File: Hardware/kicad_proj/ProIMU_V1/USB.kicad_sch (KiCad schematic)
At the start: 8 parts

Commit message: Updated Schematic and Layout
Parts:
- gave numbers to parts that had none: 8
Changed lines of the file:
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@@
   (symbol (lib_id "power:GND") (at 156.21 92.71 0) (unit 1)
     (in_bom yes) (on_board yes) (fields_autoplaced)
-    (property "Reference" "#PWR?" (id 0) (at 156.21 99.06 0)
+    (property "Reference" "#PWR0104" (id 0) (at 156.21 99.06 0)
       (effects (font (size 1.27 1.27)) hide)
     )
@@
   (symbol (lib_id "power:GND") (at 168.91 64.77 90) (mirror x) (unit 1)
     (in_bom yes) (on_board yes) (fields_autoplaced)
-    (property "Reference" "#PWR?" (id 0) (at 175.26 64.77 0)
+    (property "Reference" "#PWR0102" (id 0) (at 175.26 64.77 0)
       (effects (font (size 1.27 1.27)) hide)
     )
@@
   (symbol (lib_id "power:GND") (at 167.64 57.15 0) (unit 1)
     (in_bom yes) (on_board yes) (fields_autoplaced)
-    (property "Reference" "#PWR?" (id 0) (at 167.64 63.5 0)
+    (property "Reference" "#PWR0103" (id 0) (at 167.64 63.5 0)
       (effects (font (size 1.27 1.27)) hide)
     )
@@
   (symbol (lib_id "power:GND") (at 170.18 91.44 0) (unit 1)
     (in_bom yes) (on_board yes) (fields_autoplaced)
-    (property "Reference" "#PWR?" (id 0) (at 170.18 97.79 0)
+    (property "Reference" "#PWR0105" (id 0) (at 170.18 97.79 0)
       (effects (font (size 1.27 1.27)) hide)
     )
@@
   (symbol (lib_id "Device:R_Small") (at 167.64 50.8 0) (mirror x) (unit 1)
     (in_bom yes) (on_board yes)
-    (property "Reference" "R?" (id 0) (at 165.1 52.07 90)
+    (property "Reference" "R5" (id 0) (at 165.1 52.07 90)
       (effects (font (size 1.27 1.27)) (justify right))
     )
@@
   (symbol (lib_id "Simulation_SPICE:DIODE") (at 179.07 38.1 0) (unit 1)
     (in_bom yes) (on_board yes) (fields_autoplaced)
-    (property "Reference" "D?" (id 0) (at 179.07 31.75 0))
+    (property "Reference" "D2" (id 0) (at 179.07 31.75 0))
     (property "Value" "DIODE" (id 1) (at 179.07 34.29 0))
     (property "Footprint" "" (id 2) (at 179.07 38.1 0)
@@
   (symbol (lib_id "power:VDD") (at 193.04 34.29 0) (mirror y) (unit 1)
     (in_bom yes) (on_board yes)
-    (property "Reference" "#PWR?" (id 0) (at 193.04 38.1 0)
+    (property "Reference" "#PWR0101" (id 0) (at 193.04 38.1 0)
       (effects (font (size 1.27 1.27)) hide)
     )
@@
   (symbol (lib_id "Device:R_Small") (at 167.64 43.18 0) (mirror x) (unit 1)
     (in_bom yes) (on_board yes)
-    (property "Reference" "R?" (id 0) (at 165.1 44.45 90)
+    (property "Reference" "R4" (id 0) (at 165.1 44.45 90)
       (effects (font (size 1.27 1.27)) (justify right))
     )
@@
   (symbol (lib_id "Device:R_Small") (at 154.94 71.12 90) (mirror x) (unit 1)
     (in_bom yes) (on_board yes)
-    (property "Reference" "R?" (id 0) (at 149.86 68.58 90)
+    (property "Reference" "R1" (id 0) (at 149.86 68.58 90)
       (effects (font (size 1.27 1.27)) (justify right))
     )
@@
   (symbol (lib_id "Device:C_Small") (at 160.02 64.77 270) (unit 1)
     (in_bom yes) (on_board yes)
-    (property "Reference" "C?" (id 0) (at 158.75 63.5 90)
+    (property "Reference" "C2" (id 0) (at 158.75 63.5 90)
       (effects (font (size 1.27 1.27)) (justify right))
     )
@@
   (symbol (lib_id "Power_Protection:SP0502BAHT") (at 170.18 83.82 0) (unit 1)
     (in_bom yes) (on_board yes) (fields_autoplaced)
-    (property "Reference" "D?" (id 0) (at 176.53 82.5499 0)
+    (property "Reference" "D1" (id 0) (at 176.53 82.5499 0)
       (effects (font (size 1.27 1.27)) (justify left))
     )
@@
   (symbol (lib_id "Device:R_Small") (at 154.94 76.2 270) (mirror x) (unit 1)
     (in_bom yes) (on_board yes)
-    (property "Reference" "R?" (id 0) (at 154.94 78.74 90)
+    (property "Reference" "R2" (id 0) (at 154.94 78.74 90)
       (effects (font (size 1.27 1.27)) (justify right))
     )
@@
   (symbol (lib_id "USB4105-GF-A:USB4105-GF-A") (at 135.89 74.93 0) (unit 1)
     (in_bom yes) (on_board yes)
-    (property "Reference" "USB?" (id 0) (at 121.92 59.69 0))
+    (property "Reference" "USB1" (id 0) (at 121.92 59.69 0))
     (property "Value" "USB4105-GF-A" (id 1) (at 135.89 59.055 0))
     (property "Footprint" "footprints:GCT_USB4105-GF-A" (id 2) (at 90.17 63.5 0)

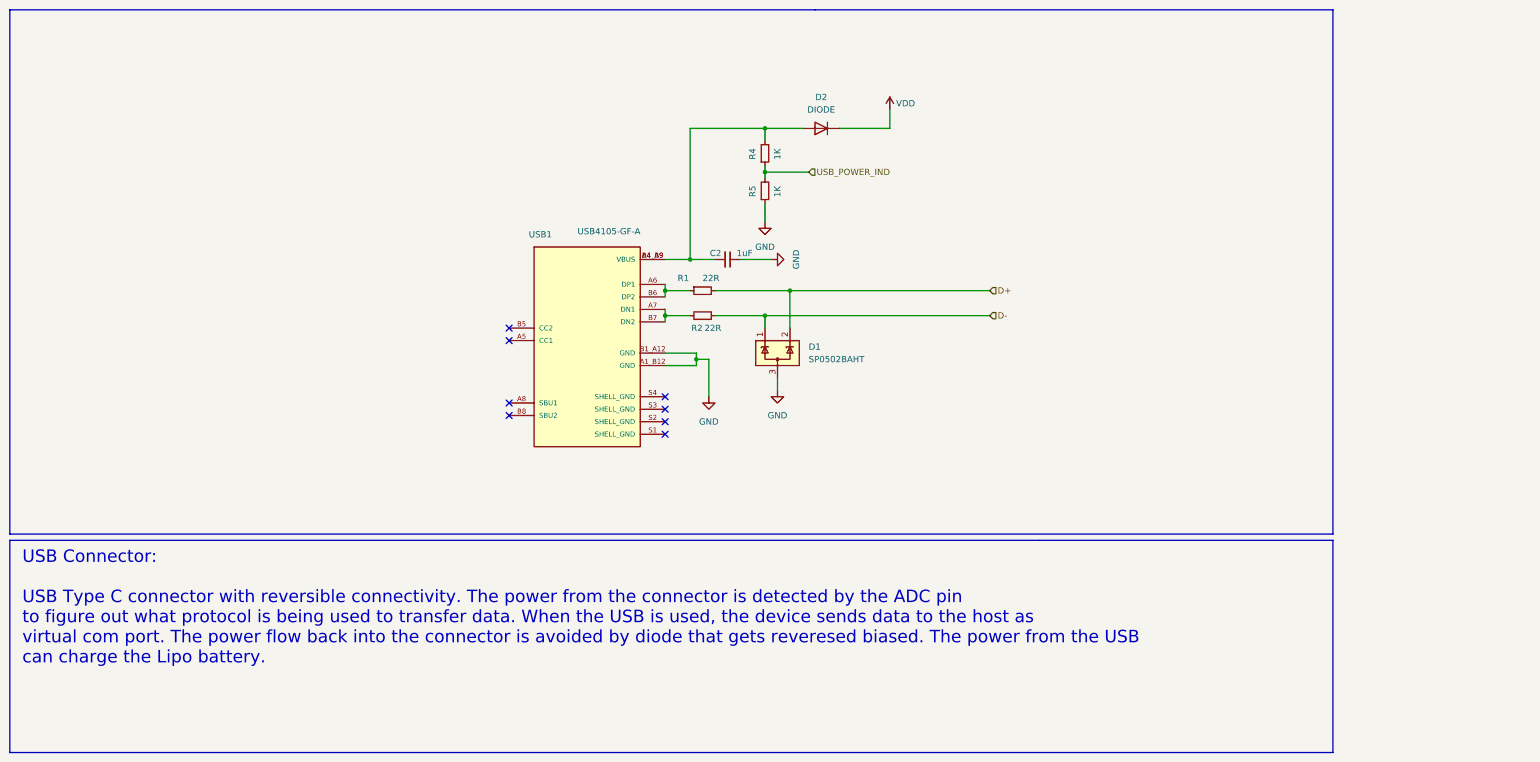
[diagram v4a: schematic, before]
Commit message: Added New USB footprint. This will be used through entire project and will not be changed
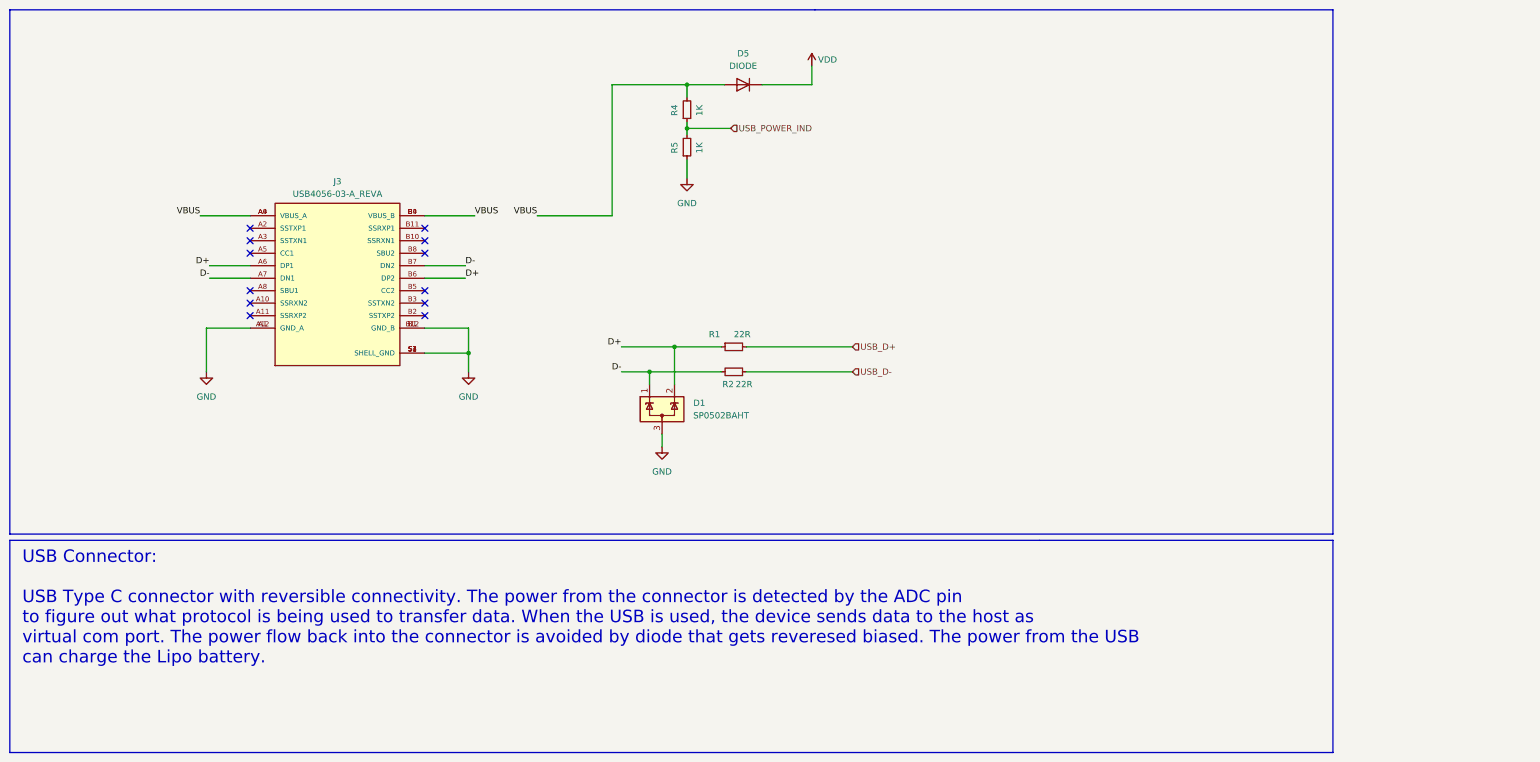
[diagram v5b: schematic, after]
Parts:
- removed C2: 1uF, Capacitor_SMD:C_0402_1005Metric_Pad0.74x0.62mm_HandSolder, symbol Device:C_Small
- removed D2: DIODE, symbol Simulation_SPICE:DIODE
- removed USB1: USB4105-GF-A, footprints:GCT_USB4105-GF-A, symbol USB4105-GF-A:USB4105-GF-A
- added D5: DIODE, symbol Simulation_SPICE:DIODE
- added J3: USB4056-03-A_REVA, GCT_USB4056-03-A_REVA, symbol USB4056-03-A_REVA:USB4056-03-A_REVA
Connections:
- net D+: now also R1.1, J3.A6 (DP1), J3.B6 (DP2); no longer R1.2
- net D-: now also R2.2, J3.A7 (DN1), J3.B7 (DN2); no longer R2.1
- net GND: now also J3.A1 (GND_A), J3.A12 (GND_A), J3.B1 (GND_B), J3.B12 (GND_B), J3.S1 (SHELL_GND), J3.S2 (SHELL_GND), J3.S3 (SHELL_GND), J3.S4 (SHELL_GND)
- net VDD: now also D5.2 (K)
- net VBUS: now reaches R4.2
- net VBUS: now also D5.1 (A), J3.A4 (VBUS_A), J3.A9 (VBUS_A), J3.B4 (VBUS_B), J3.B9 (VBUS_B)
- new net USB_D+: R1.2
- new net USB_D-: R2.1
- no-connect marks 8 -> 12
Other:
- moved on the sheet: D1, R1, R2, R4, R5

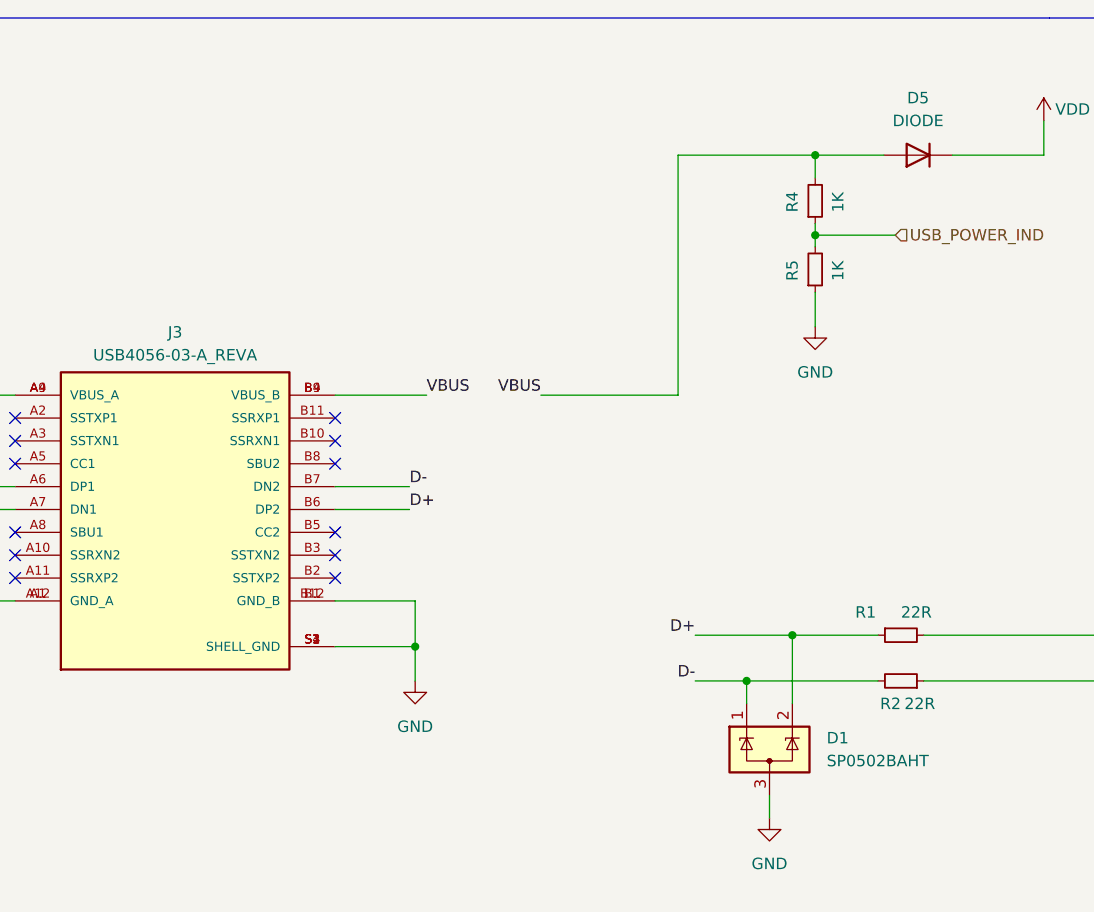
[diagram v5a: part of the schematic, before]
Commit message: Updated schematic and layout
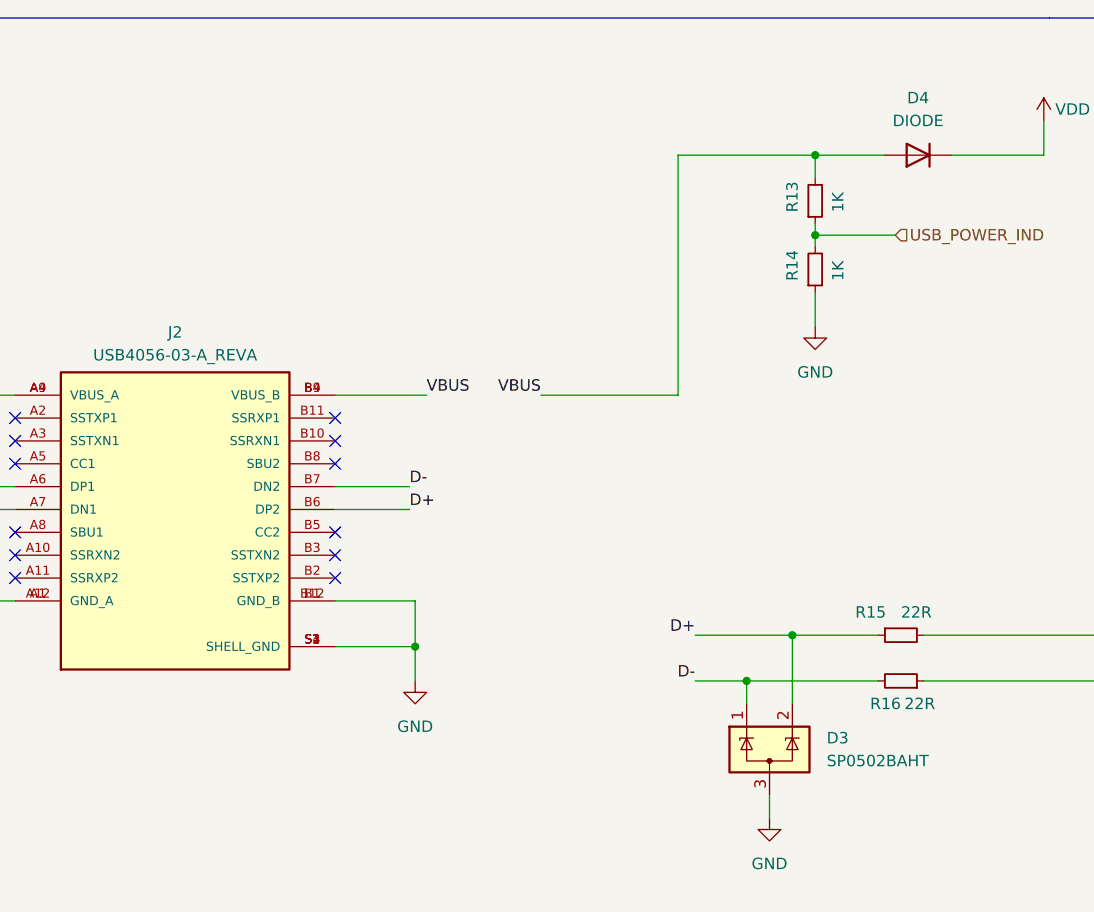
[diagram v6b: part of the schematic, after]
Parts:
- renumbered D1 to D3, D5 to D4, J3 to J2, R4 to R13, R5 to R14, R1 to R15, R2 to R16
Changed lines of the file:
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@@
   (symbol (lib_id "power:GND") (at 107.315 87.63 0) (unit 1)
     (in_bom yes) (on_board yes) (fields_autoplaced)
-    (property "Reference" "#PWR02" (id 0) (at 107.315 93.98 0)
+    (property "Reference" "#PWR062" (id 0) (at 107.315 93.98 0)
       (effects (font (size 1.27 1.27)) hide)
     )
@@
   (symbol (lib_id "power:GND") (at 151.765 48.26 0) (unit 1)
     (in_bom yes) (on_board yes) (fields_autoplaced)
-    (property "Reference" "#PWR0103" (id 0) (at 151.765 54.61 0)
+    (property "Reference" "#PWR064" (id 0) (at 151.765 54.61 0)
       (effects (font (size 1.27 1.27)) hide)
     )
@@
   (symbol (lib_id "power:GND") (at 146.685 102.87 0) (unit 1)
     (in_bom yes) (on_board yes) (fields_autoplaced)
-    (property "Reference" "#PWR0105" (id 0) (at 146.685 109.22 0)
+    (property "Reference" "#PWR063" (id 0) (at 146.685 109.22 0)
       (effects (font (size 1.27 1.27)) hide)
     )
@@
   (symbol (lib_id "Simulation_SPICE:DIODE") (at 163.195 29.21 0) (unit 1)
     (in_bom yes) (on_board yes) (fields_autoplaced)
-    (property "Reference" "D5" (id 0) (at 163.195 22.86 0))
+    (property "Reference" "D4" (id 0) (at 163.195 22.86 0))
     (property "Value" "DIODE" (id 1) (at 163.195 25.4 0))
     (property "Footprint" "" (id 2) (at 163.195 29.21 0)
@@
   (symbol (lib_id "Device:R_Small") (at 151.765 41.91 0) (mirror x) (unit 1)
     (in_bom yes) (on_board yes)
-    (property "Reference" "R5" (id 0) (at 149.225 43.18 90)
+    (property "Reference" "R14" (id 0) (at 149.225 43.18 90)
       (effects (font (size 1.27 1.27)) (justify right))
     )
@@
   (symbol (lib_id "USB4056-03-A_REVA:USB4056-03-A_REVA") (at 80.645 68.58 0) (unit 1)
     (in_bom yes) (on_board yes) (fields_autoplaced)
-    (property "Reference" "J3" (id 0) (at 80.645 48.895 0))
+    (property "Reference" "J2" (id 0) (at 80.645 48.895 0))
     (property "Value" "USB4056-03-A_REVA" (id 1) (at 80.645 51.435 0))
     (property "Footprint" "GCT_USB4056-03-A_REVA" (id 2) (at 80.645 68.58 0)
@@
   (symbol (lib_id "power:VDD") (at 177.165 25.4 0) (mirror y) (unit 1)
     (in_bom yes) (on_board yes)
-    (property "Reference" "#PWR0101" (id 0) (at 177.165 29.21 0)
+    (property "Reference" "#PWR065" (id 0) (at 177.165 29.21 0)
       (effects (font (size 1.27 1.27)) hide)
     )
@@
   (symbol (lib_id "Device:R_Small") (at 151.765 34.29 0) (mirror x) (unit 1)
     (in_bom yes) (on_board yes)
-    (property "Reference" "R4" (id 0) (at 149.225 35.56 90)
+    (property "Reference" "R13" (id 0) (at 149.225 35.56 90)
       (effects (font (size 1.27 1.27)) (justify right))
     )
@@
   (symbol (lib_id "power:GND") (at 53.975 87.63 0) (mirror y) (unit 1)
     (in_bom yes) (on_board yes) (fields_autoplaced)
-    (property "Reference" "#PWR01" (id 0) (at 53.975 93.98 0)
+    (property "Reference" "#PWR061" (id 0) (at 53.975 93.98 0)
       (effects (font (size 1.27 1.27)) hide)
     )
@@
   (symbol (lib_id "Device:R_Small") (at 161.29 82.55 90) (mirror x) (unit 1)
     (in_bom yes) (on_board yes)
-    (property "Reference" "R1" (id 0) (at 156.21 80.01 90)
+    (property "Reference" "R15" (id 0) (at 156.21 80.01 90)
       (effects (font (size 1.27 1.27)) (justify right))
     )
@@
   (symbol (lib_id "Power_Protection:SP0502BAHT") (at 146.685 95.25 0) (unit 1)
     (in_bom yes) (on_board yes) (fields_autoplaced)
-    (property "Reference" "D1" (id 0) (at 153.035 93.9799 0)
+    (property "Reference" "D3" (id 0) (at 153.035 93.9799 0)
       (effects (font (size 1.27 1.27)) (justify left))
     )
@@
   (symbol (lib_id "Device:R_Small") (at 161.29 87.63 270) (mirror x) (unit 1)
     (in_bom yes) (on_board yes)
-    (property "Reference" "R2" (id 0) (at 161.29 90.17 90)
-      (effects (font (size 1.27 1.27)) (justify right))
-    )
+    (property "Reference" "R16" (id 0) (at 161.29 90.17 90)
+      (effects (font (size 1.27 1.27)) (justify right))
+    )

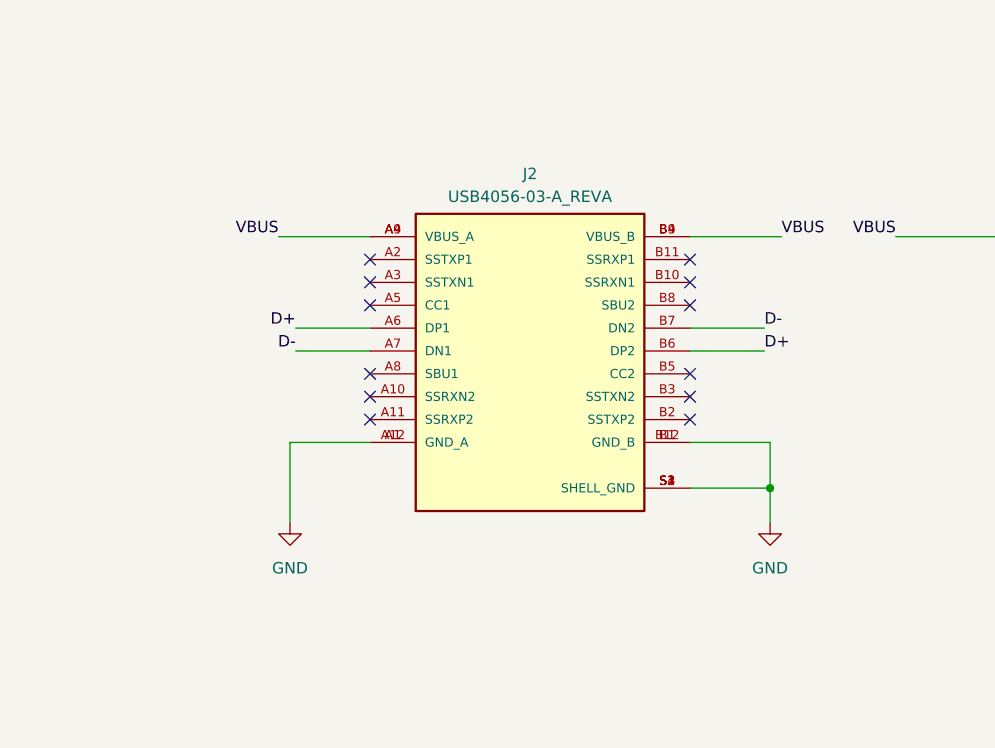
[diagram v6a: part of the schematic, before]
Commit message: Added a completed GPS V1 Schematic
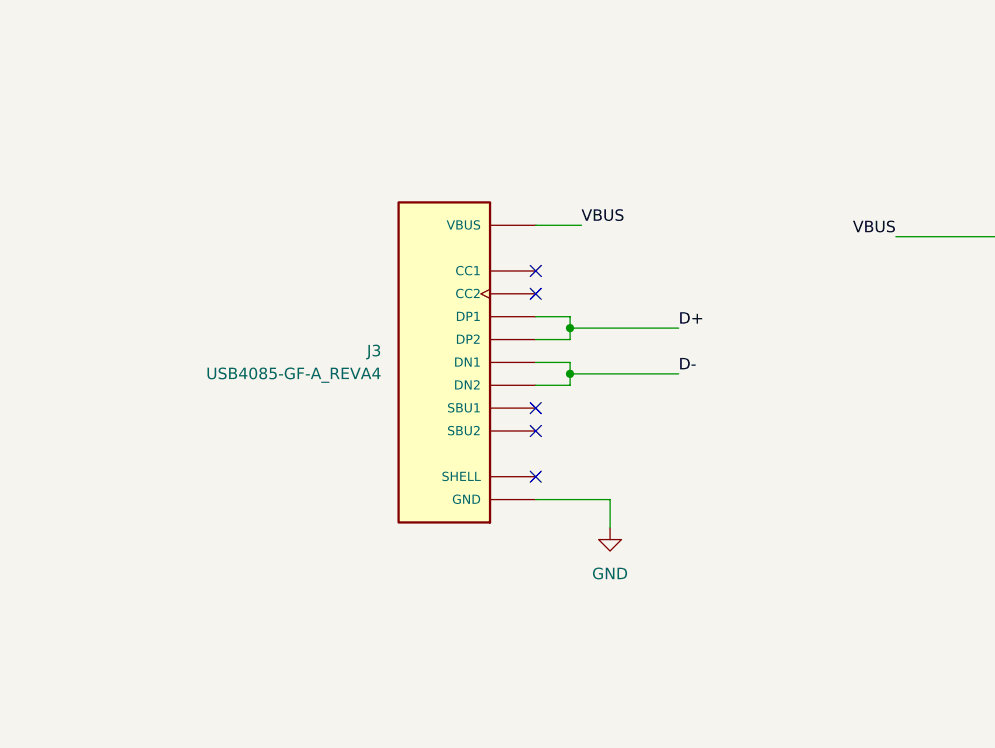
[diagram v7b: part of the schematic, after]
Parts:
- removed J2: USB4056-03-A_REVA, GCT_USB4056-03-A_REVA, symbol USB4056-03-A_REVA:USB4056-03-A_REVA
- added J3: USB4085-GF-A_REVA4, footprints:GCT_USB4085-GF-A_REVA4, symbol USB4085-GF-A_REVA4:USB4085-GF-A_REVA4
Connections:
- net D+: now also J3.A6 (DP1), J3.B6 (DP2)
- net D-: now also J3.A7 (DN1), J3.B7 (DN2)
- net GND: now also J3.A1 (GND), J3.A12 (GND), J3.B1 (GND), J3.B12 (GND)
- net VBUS: now also J3.A4 (VBUS), J3.A9 (VBUS), J3.B4 (VBUS), J3.B9 (VBUS)
- new net: J3.P1 (SHELL), J3.P2 (SHELL), J3.P3 (SHELL), J3.P4 (SHELL)
- no-connect marks 12 -> 5
